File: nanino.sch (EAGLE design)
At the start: 19 parts, among them IC1 ATMEGA168-20P

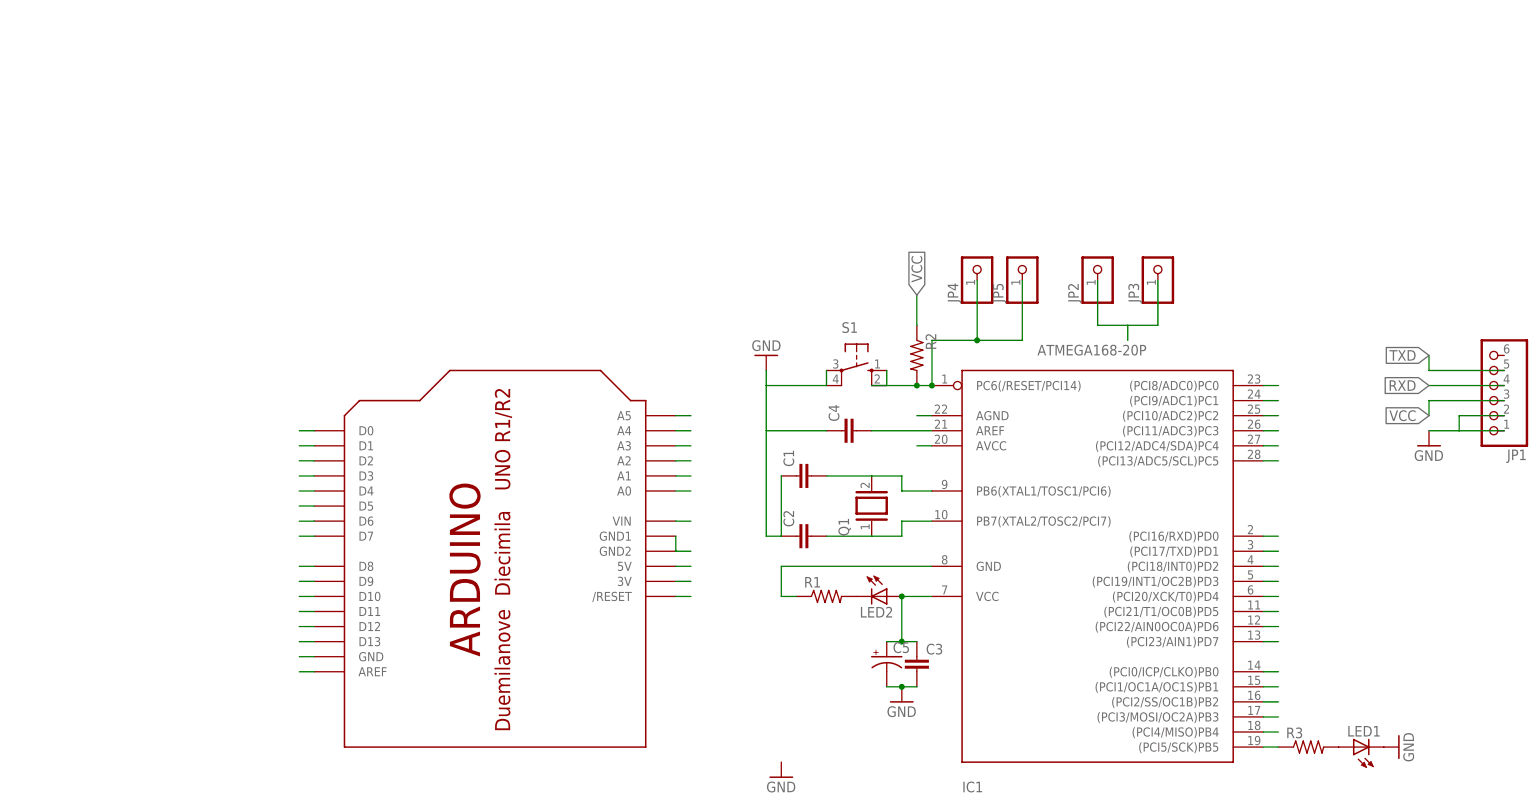
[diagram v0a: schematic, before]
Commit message: Fablab Imperia fork
Some minor moves, added some clearance, added groundplane, prototyping
zone like the Nanino, some reference values and the text
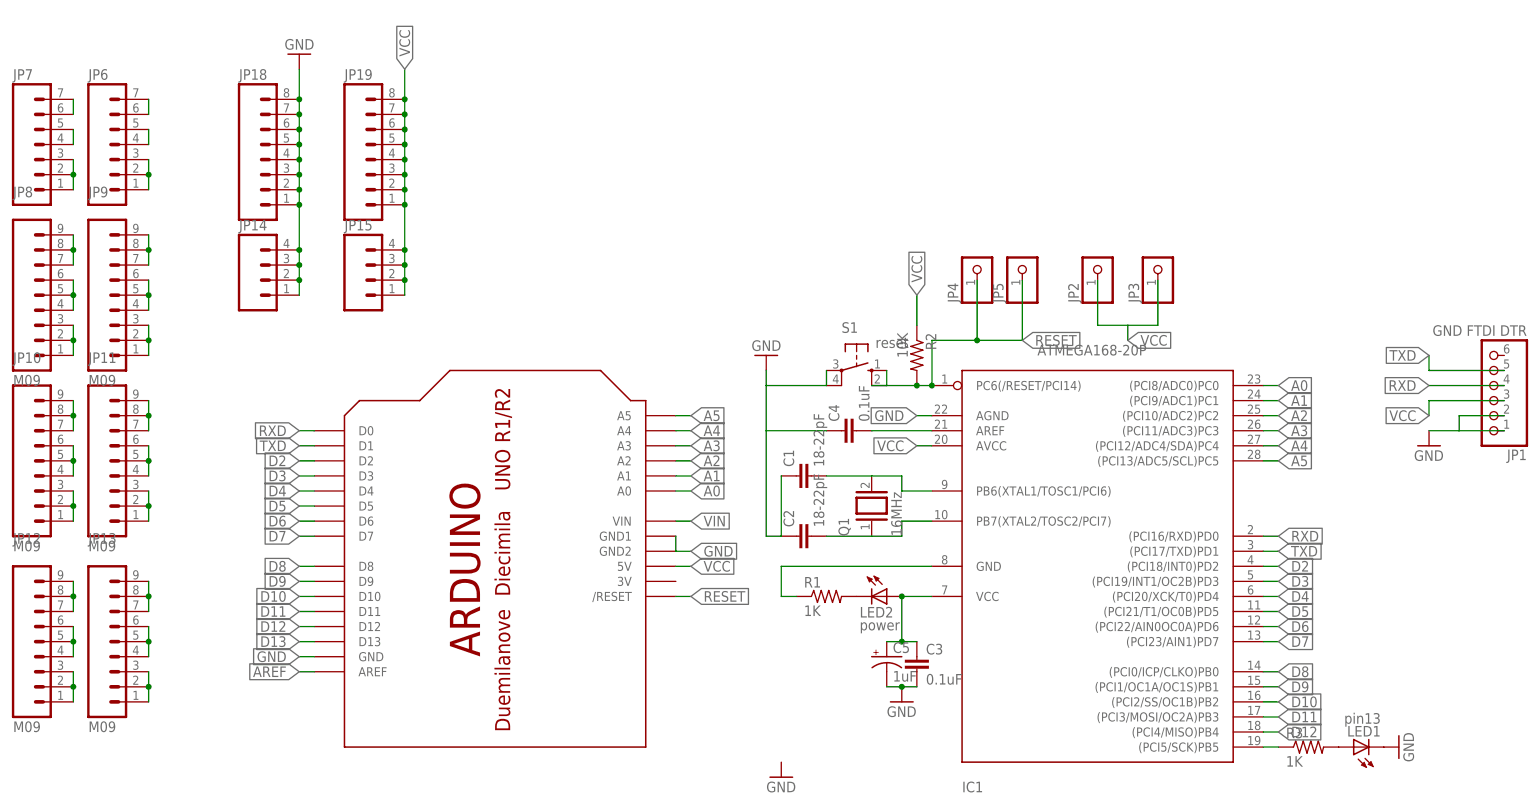
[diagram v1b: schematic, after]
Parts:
- added JP10, JP11, JP12, JP13, JP8, JP9: M09, SparkFun-Connectors:M09
- added JP14, JP15: (no value), SparkFun-Connectors:M04PTH
- added JP18, JP19: (no value), SparkFun-Connectors:M081X08
- added JP6, JP7: (no value), SparkFun-Connectors:M07
- C1, C2: value (none) -> 18-22pF
- C3, C4: value (none) -> 0.1uF
- C5: value (none) -> 1uF
- JP1: value (none) -> GND FTDI DTR
- LED1: value (none) -> pin13
- LED2: value (none) -> power
- Q1: value (none) -> 16MHz
- R1, R3: value (none) -> 1K
- R2: value (none) -> 10K
- S1: value (none) -> reset
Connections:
- new net N$10: JP11.4, JP11.5, JP11.6
- new net N$12: JP13.1, JP13.2, JP13.3
- new net N$13: JP13.4, JP13.5, JP13.6
- new net N$14: JP13.7, JP13.8, JP13.9
- new net N$15: JP12.1, JP12.2, JP12.3
- new net N$16: JP12.4, JP12.5, JP12.6
- new net N$17: JP12.7, JP12.8, JP12.9
- new net N$18: JP10.1, JP10.2, JP10.3
- new net N$19: JP10.4, JP10.5, JP10.6
- new net N$20: JP10.7, JP10.8, JP10.9
- new net N$21: JP8.1, JP8.2, JP8.3
- new net N$22: JP8.4, JP8.5, JP8.6
- new net N$23: JP8.7, JP8.8, JP8.9
- new net N$24: JP6.1, JP6.2, JP6.3
- new net N$25: JP6.6, JP6.7
- new net N$26: JP7.1, JP7.2, JP7.3
- new net N$27: JP7.6, JP7.7
- new net N$28: JP6.4, JP6.5
- new net N$29: JP7.4, JP7.5
- new net N$5: JP9.1, JP9.2, JP9.3
- new net N$7: JP9.4, JP9.5, JP9.6
- new net N$8: JP9.7, JP9.8, JP9.9
- new net N$9: JP11.1, JP11.2, JP11.3
- net GND: now also JP14.1, JP14.2, JP14.3, JP14.4, JP18.1, JP18.2, JP18.3, JP18.4, JP18.5, JP18.6, JP18.7, JP18.8
- net N$11: now also JP11.7, JP11.8, JP11.9; no longer U$1.3V
- net VCC: now also JP15.1, JP15.2, JP15.3, JP15.4, JP19.1, JP19.2, JP19.3, JP19.4, JP19.5, JP19.6, JP19.7, JP19.8
